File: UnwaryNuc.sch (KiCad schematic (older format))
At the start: 174 parts, among them J1 USB_B_Micro, J2 USB_A_Dual, J3 Conn_01x06_Male, J4 RJ45_Amphenol_RJMG1BD3B8K1ANR, J5 RJ45_Amphenol_RJMG1BD3B8K1ANR, J6 Conn_02x04_Odd_Even, Q1 2N3904, Q2 BC856BDW1, SW1 SW_SPST, U1 NUC980DF71YC, U2 LAN8740A-EN-TR, U3 LAN8740A-EN-TR, U4 LD3985M18R_TSOT23, U5 MIC4690, U6 LM3880, U7 AP2127K-1.2, U8 S25FL127SABMFV100, X1 ASE-xxxMHz, X2 ASE-xxxMHz, Y1 ABS07-166, Y2 NX5032GA

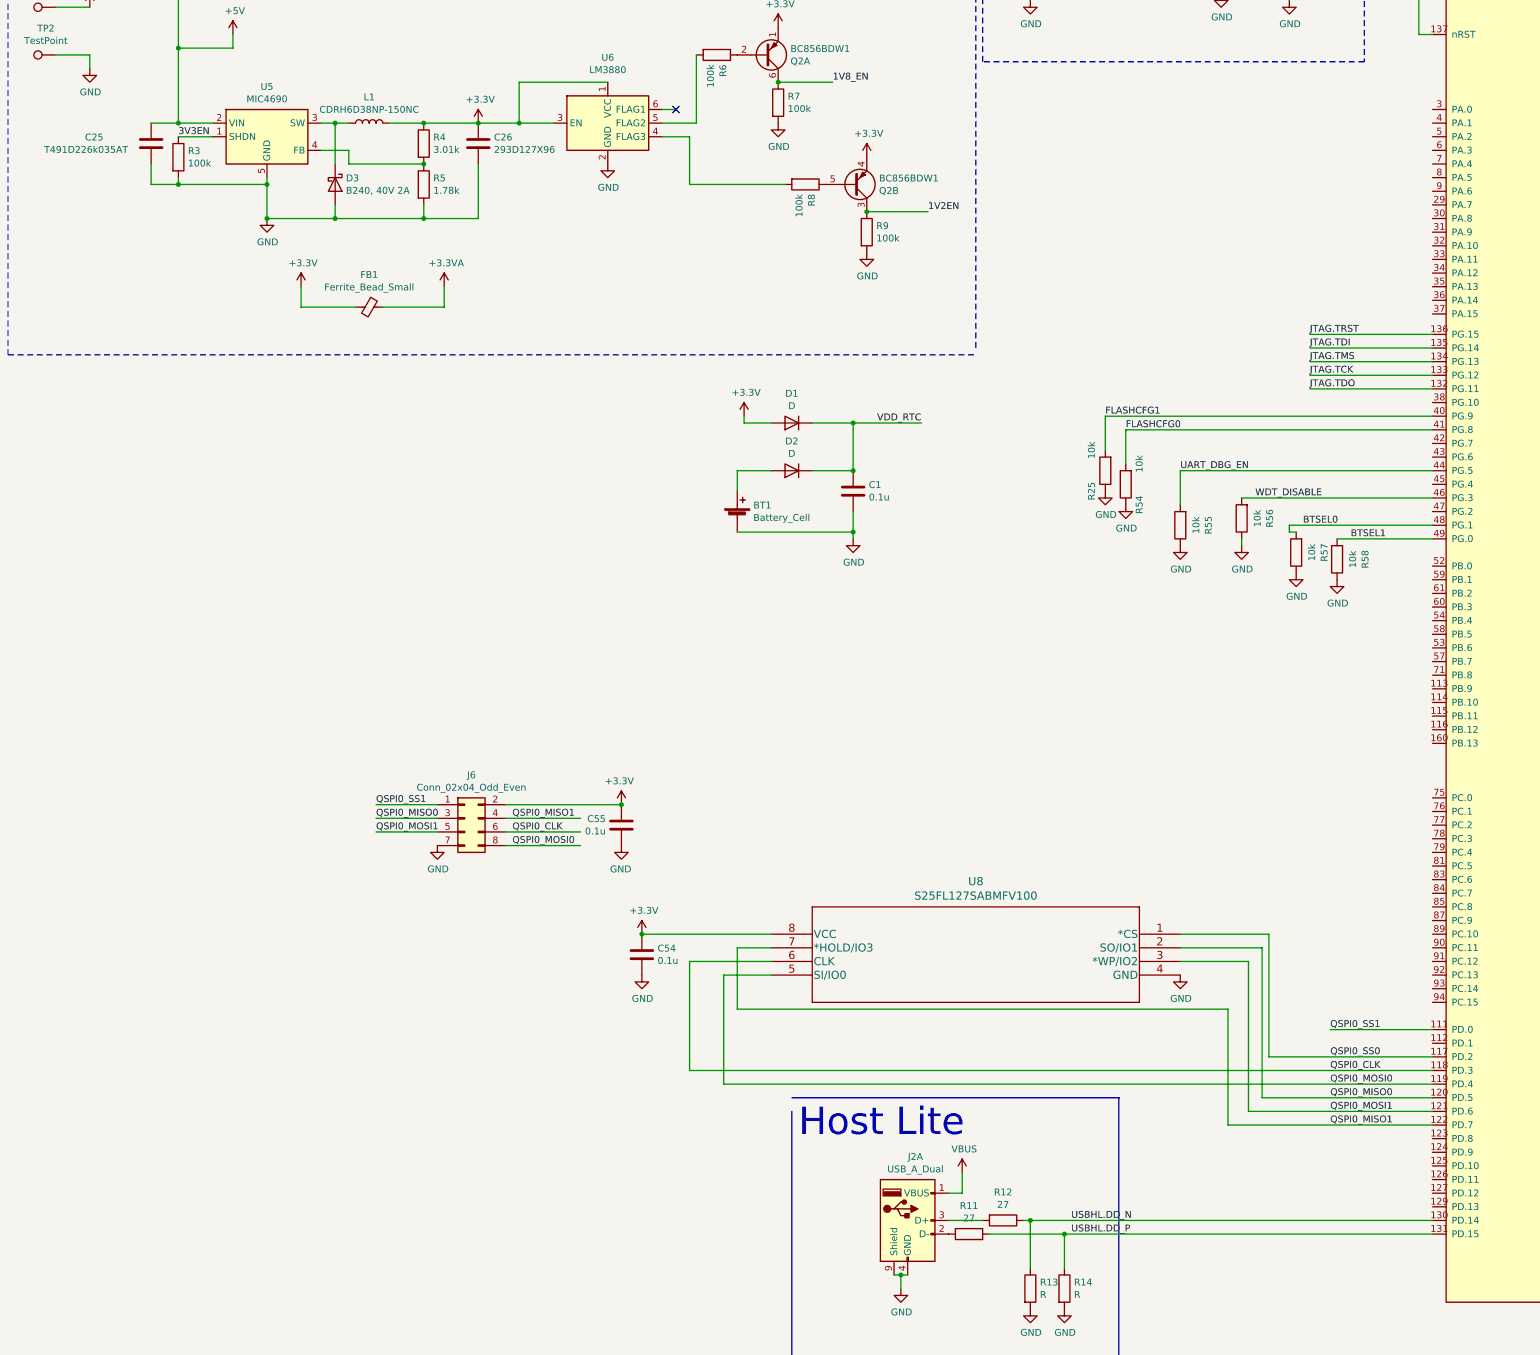
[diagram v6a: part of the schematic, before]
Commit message: added two spi headers, I2C, and a bank of GPIO. placed, still need routed
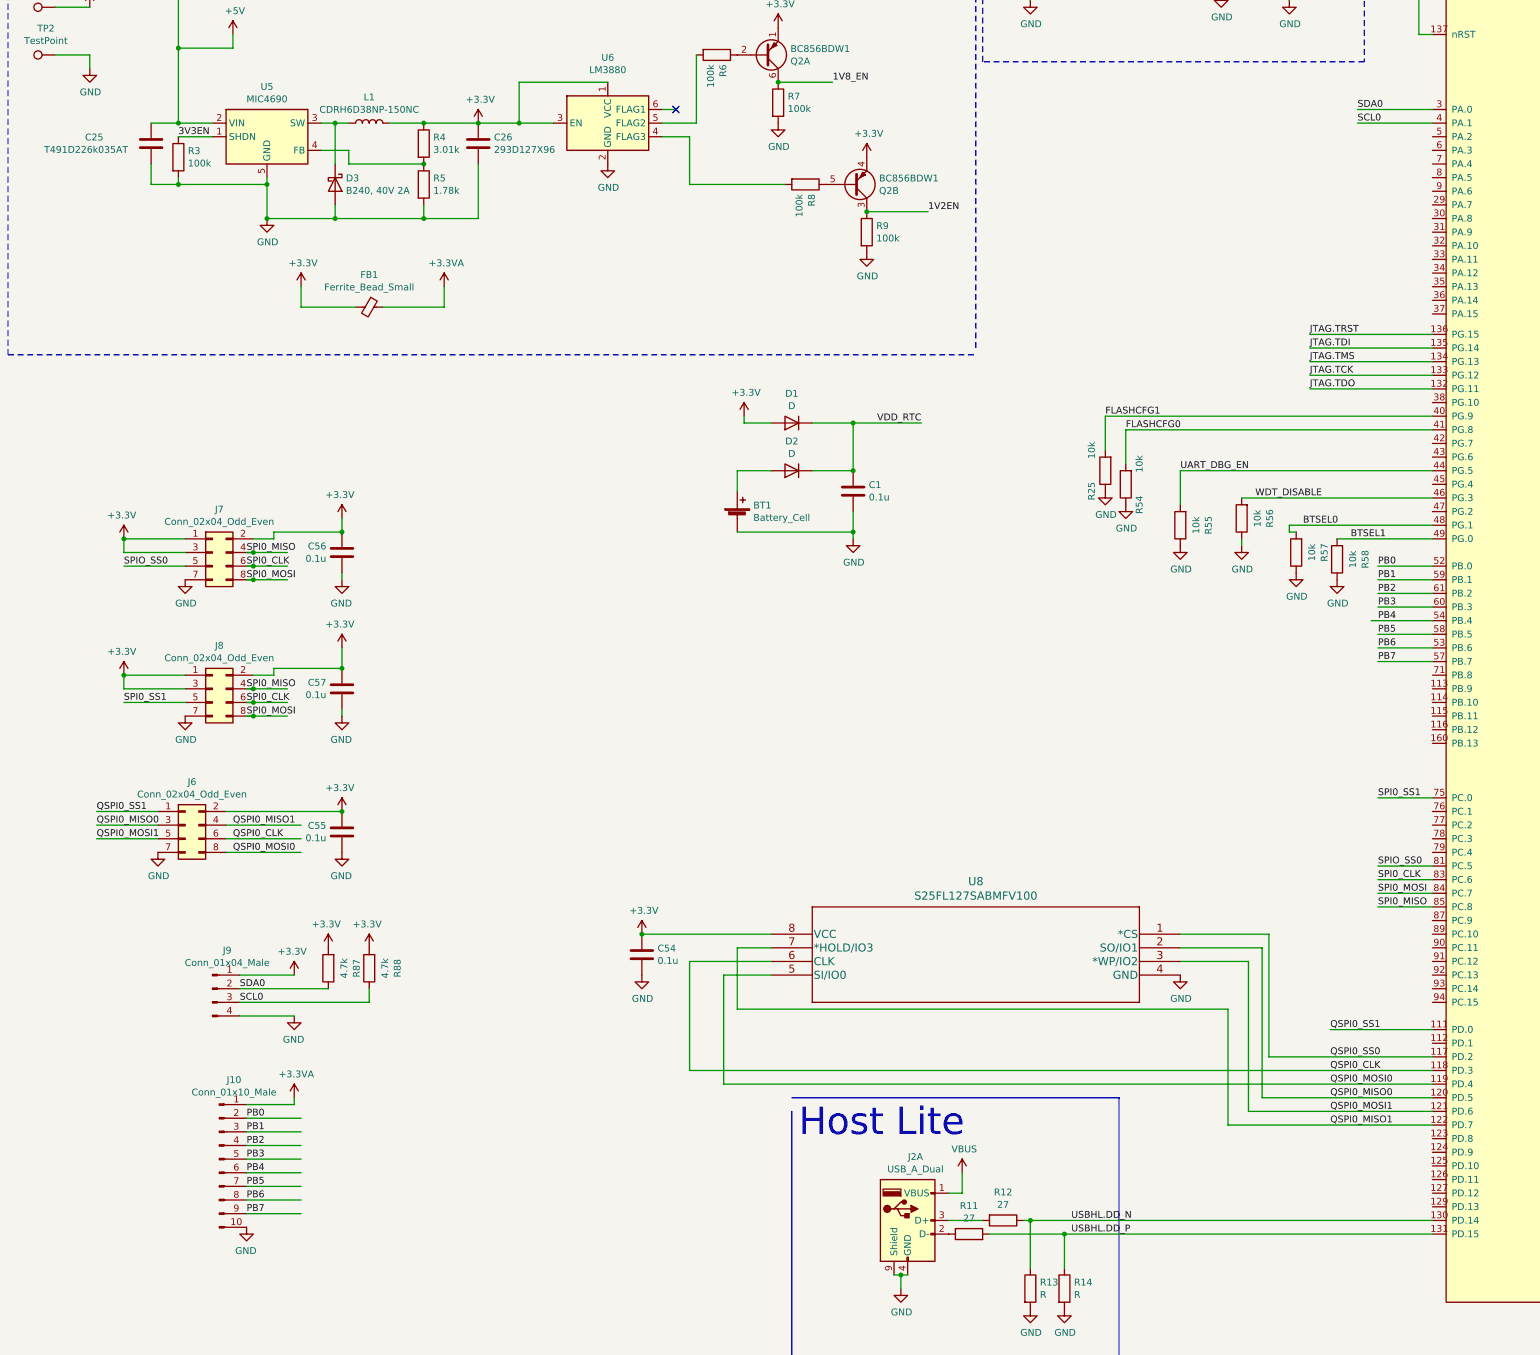
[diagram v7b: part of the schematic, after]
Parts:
- added C56, C57: 0.1u, Capacitor_SMD:C_1206_3216Metric_Pad1.33x1.80mm_HandSolder, symbol Device:C
- added J10: Conn_01x10_Male, Connector_PinHeader_2.54mm:PinHeader_1x10_P2.54mm_Vertical, symbol Connector:Conn_01x10_Male
- added J7, J8: Conn_02x04_Odd_Even, Connector_PinHeader_2.54mm:PinHeader_2x04_P2.54mm_Vertical, symbol Connector_Generic:Conn_02x04_Odd_Even
- added J9: Conn_01x04_Male, Connector_PinHeader_2.54mm:PinHeader_1x04_P2.54mm_Vertical, symbol Connector:Conn_01x04_Male
- added R87, R88: 4.7k, Resistor_SMD:R_0603_1608Metric_Pad0.98x0.95mm_HandSolder, symbol Device:R
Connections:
- net labels added: PB0, PB1, PB2, PB3, PB4, PB5, PB6, PB7, SCL0, SDA0, SPI0_CLK, SPI0_MISO, SPI0_MOSI, SPI0_SS1, SPIO_SS0
- wire segments 619 -> 679
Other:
- moved on the sheet: C55, J6
